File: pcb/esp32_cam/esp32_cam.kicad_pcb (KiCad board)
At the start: 2 copper layers, 31 x 43 mm, 51 parts, among them J1 Cam_Connector, J2 ESP32CAM_P1, J3 microSD_esp32Cam, J4 ESP32CAM_P2, Q1 S8050, Q2 PMOS, U1 ESP32-S(CAM), U2 ESP-PSRAM32

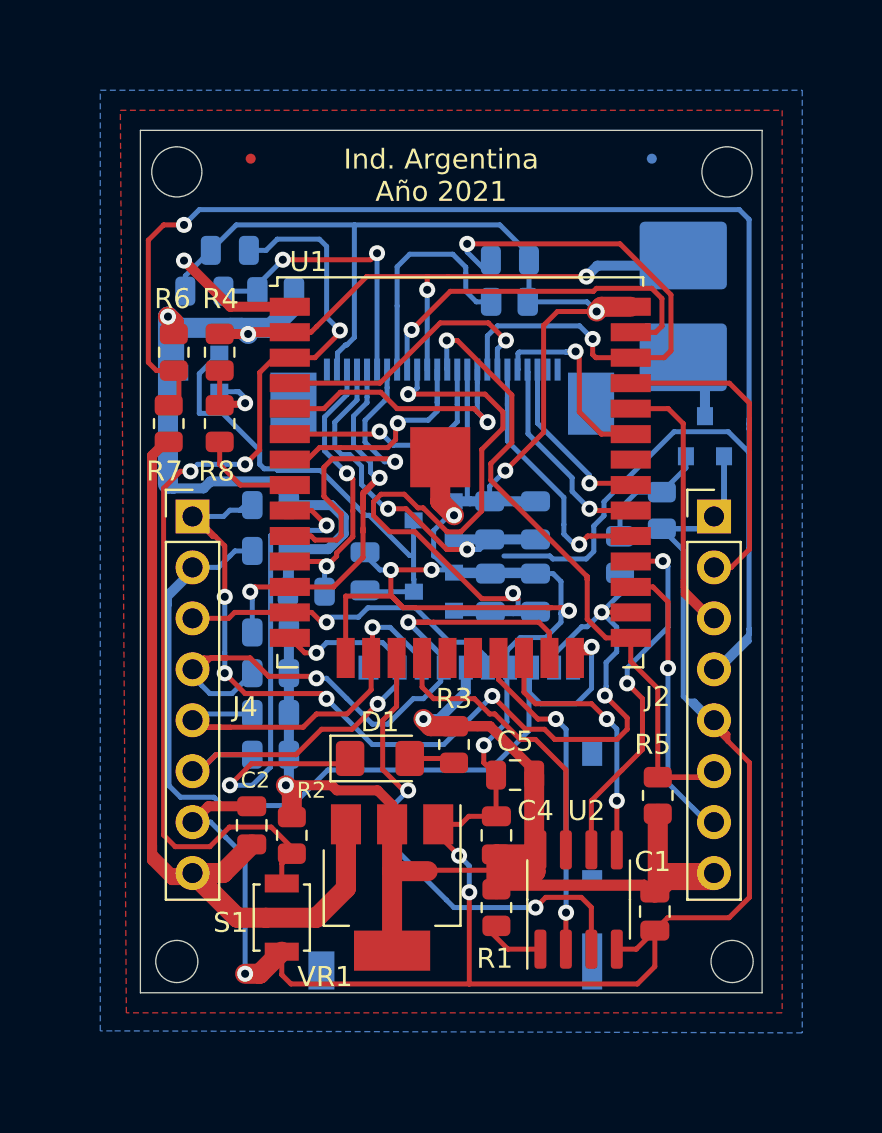
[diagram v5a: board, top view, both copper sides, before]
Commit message: se amplia el clearence de 0.2  0.25
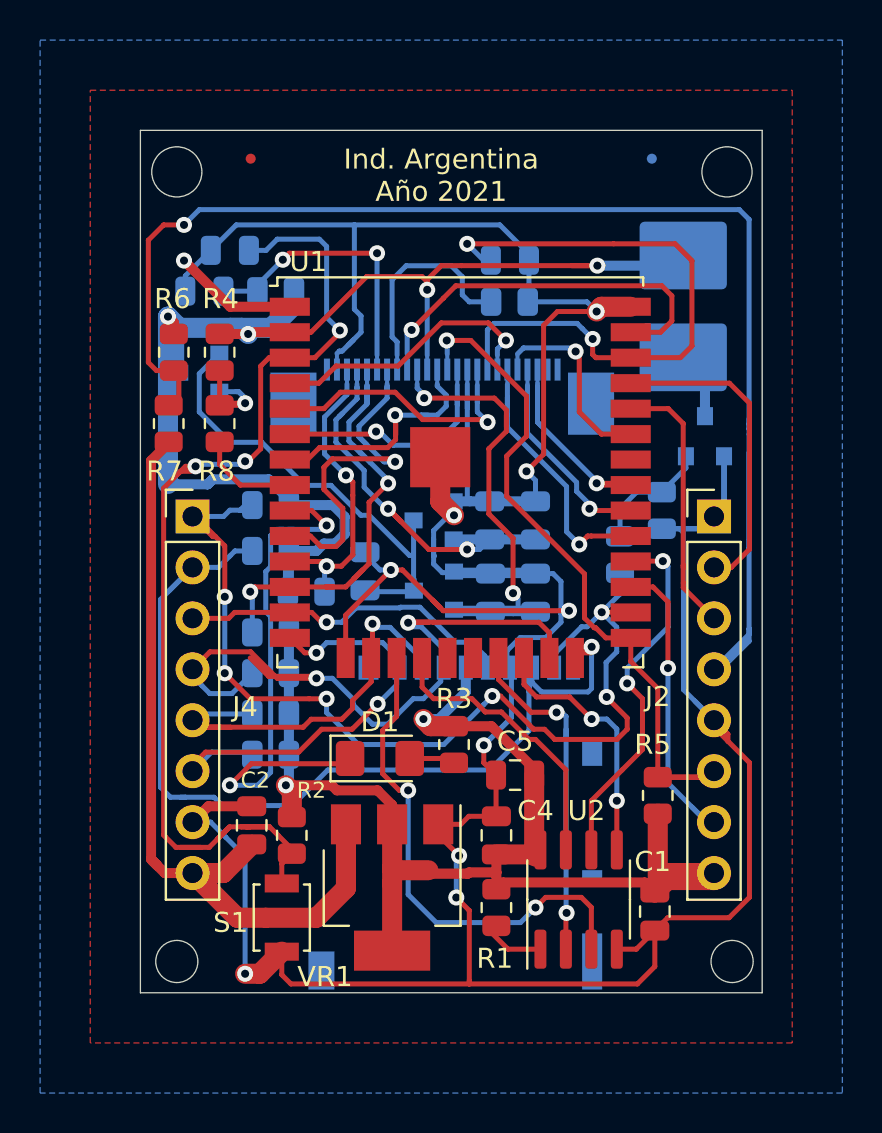
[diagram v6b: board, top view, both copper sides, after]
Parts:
- moved VR3 0.05 mm to (64.6, 75.0)
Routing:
- net Net-(J2-Pad4): track 88.3 -> 71.8 mm
- net +3V3: track 175.2 -> 162.1 mm
- net +1V2: track 37.1 -> 26.8 mm
- net Net-(C3-Pad2): track 50.2 -> 54.7 mm
- net /TWI_SCK: track 21.1 -> 25.0 mm
- net Net-(C11-Pad1): track 28.0 -> 31.0 mm
- net Net-(J2-Pad3): track 16.2 -> 13.4 mm
- net +5V: track 42.5 -> 40.2 mm
- net Net-(J1-Pad18): track 16.3 -> 18.5 mm
- net +2V8: track 19.0 -> 20.8 mm
- net GND: track 212.2 -> 210.6 mm, vias 11 -> 10
- net Net-(J1-Pad3): track 9.36 -> 10.6 mm
- net Net-(D1-Pad1): track 25.6 -> 26.8 mm
- net /HS2_DATA2: track 24.6 -> 23.5 mm
- net /TWI_SDA: track 14.8 -> 15.9 mm
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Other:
- net class Default: clearance 0.2 -> 0.25
- rule pad_to_mask_clearance: 0 -> 0.25
- rule trace_clearance: 0.2 -> 0.25
- board text added: "- DESTINATARIO DEL PRODUCTO : GERMÁN E. CARDOZO - FECHA 16/08/2021 - CONTROLES REALIZADOS BAJO STANDARD IPC– A-600 (CLASE 2) - MATERIAL, TIPO Y ESPESOR: Fr4, DOBLE FAZ, 1.60mm. - LAMINADO Y COBRE: Cu.: 1 - 1 Oz. - ESPESOR DE COBRE TOTAL EN LAS CAPAS EXTERIORES: 55µm - TERMINACIÓN DE SUPERFICIE: HASL"
- board text removed: "DATOS DEL FABRICANTE: Circuitos Impresos SEI Gavilán 3660 (1419) Buenos Aires – Argentina Tel/Fax: 4574-5009 / 4573-5807 E-mail: info@seicircuits.com Web site: www.seicircuits.com.ar DESTINATARIO DEL PRODUCTO : GERMÁN E. CARDOZO FECHA 16/08/2021 NOMBRE DEL PRODUCTO/ INSUMO: Circuito Impreso Doble Faz - PCB CÓDIGO DEL INSUMO Código cliente: Réplica ESP32-CAM ESPECIFICACIÓN Según Gerbers CONTROLES 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"
